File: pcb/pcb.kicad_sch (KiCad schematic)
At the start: 6 parts, among them U1 ESP32-S3, U2 LM337_TO220

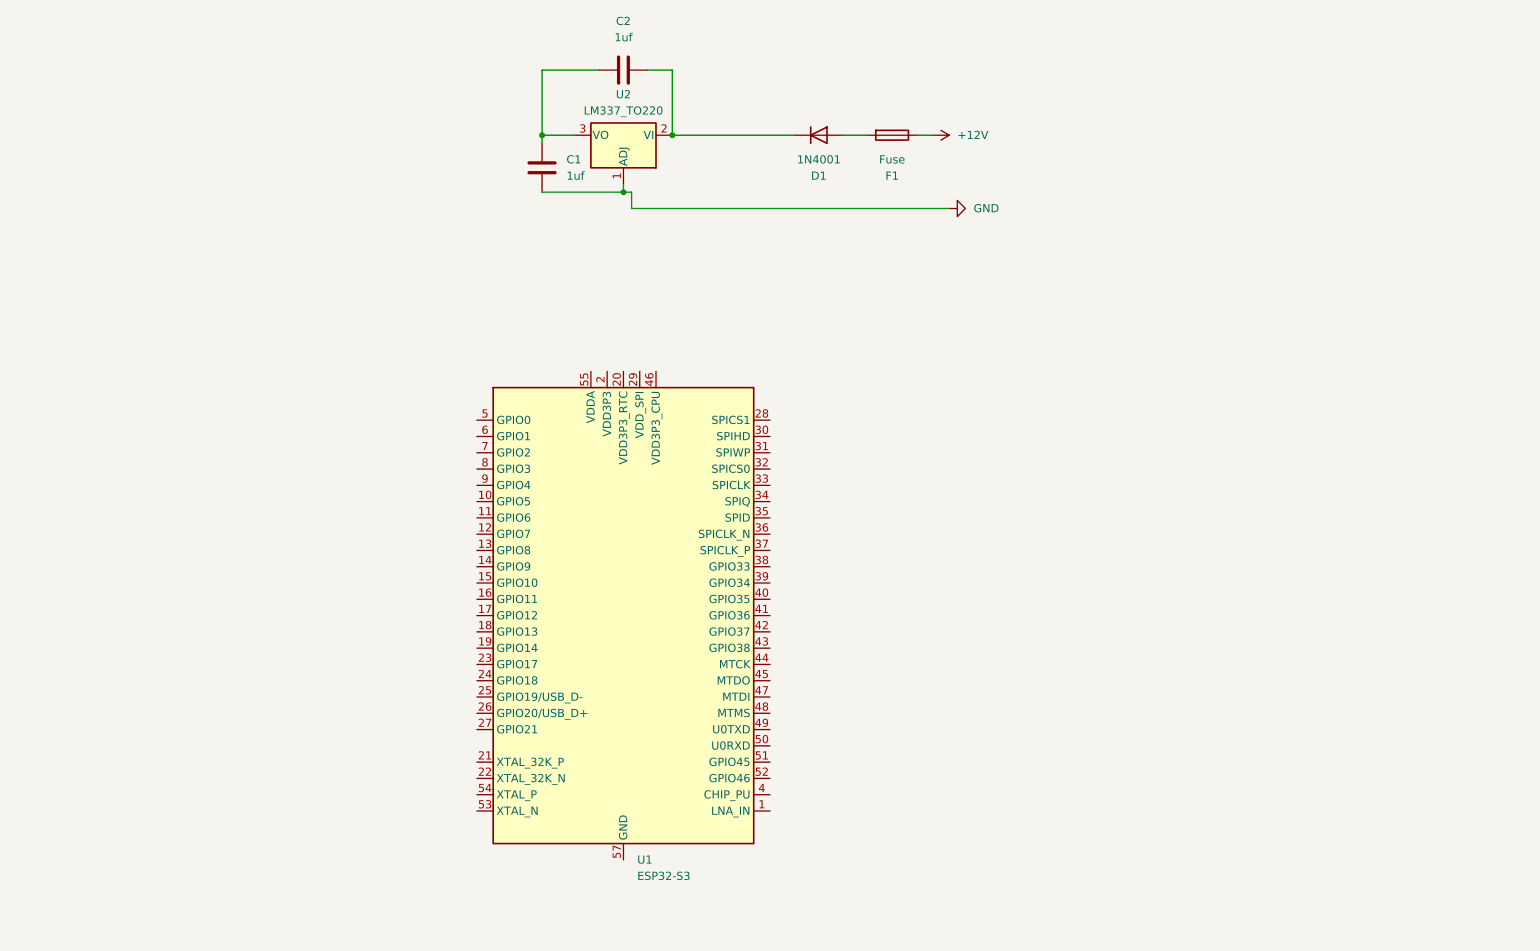
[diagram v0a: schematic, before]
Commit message: missed a wire, put more names for screw terminals
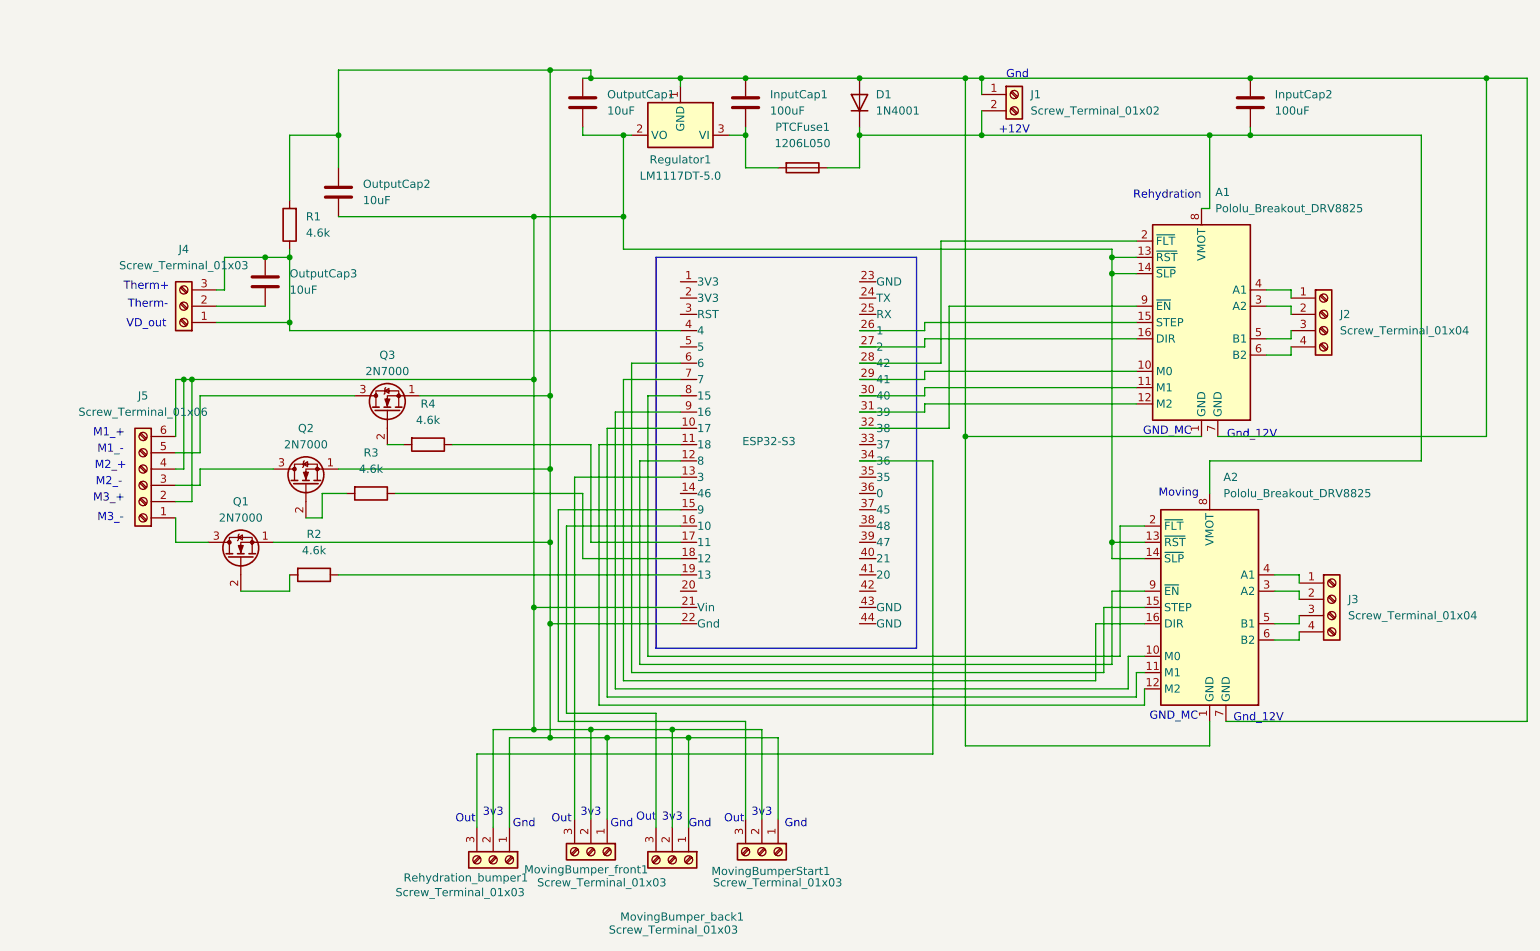
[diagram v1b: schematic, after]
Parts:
- removed C2: 1uf, Capacitor_SMD:C_01005_0402Metric, symbol Device:C
- removed U1: ESP32-S3, Package_DFN_QFN:QFN-56-1EP_7x7mm_P0.4mm_EP4x4mm, symbol MCU_Espressif:ESP32-S3
- removed U2: LM337_TO220, Package_TO_SOT_THT:TO-220-3_Vertical, symbol Regulator_Linear:LM337_TO220
- added A1, A2: Pololu_Breakout_DRV8825, Module:Pololu_Breakout-16_15.2x20.3mm, symbol Driver_Motor:Pololu_Breakout_DRV8825
- added ESP32-S3: ~, my_footprints:ESP32_DevKitC_Header_Mount, symbol symbol_libraru:ESP32-S3_DevKitC_dual_header
- added InputCap2: 100uF, Capacitor_SMD:C_0805_2012Metric, symbol Device:C
- added J1: Screw_Terminal_01x02, TerminalBlock:TerminalBlock_MaiXu_MX126-5.0-02P_1x02_P5.00mm, symbol Connector:Screw_Terminal_01x02
- added J2, J3: Screw_Terminal_01x04, TerminalBlock:TerminalBlock_MaiXu_MX126-5.0-04P_1x04_P5.00mm, symbol Connector:Screw_Terminal_01x04
- added J4, MovingBumperStart1, MovingBumper_back1, MovingBumper_front1, Rehydration_bumper1: Screw_Terminal_01x03, TerminalBlock:TerminalBlock_MaiXu_MX126-5.0-03P_1x03_P5.00mm, symbol Connector:Screw_Terminal_01x03
- added J5: Screw_Terminal_01x06, TerminalBlock:TerminalBlock_MaiXu_MX126-5.0-06P_1x06_P5.00mm, symbol Connector:Screw_Terminal_01x06
- added OutputCap1, OutputCap2, OutputCap3: 10uF, Capacitor_SMD:C_0805_2012Metric, symbol Device:C
- added Q1, Q2, Q3: 2N7000, Package_TO_SOT_THT:TO-92_Inline, symbol Transistor_FET:2N7000
- added R1, R2, R3, R4: 4.6k, Resistor_SMD:R_0805_2012Metric, symbol Device:R
- added Regulator1: LM1117DT-5.0, Package_TO_SOT_SMD:TO-252-3_TabPin2, symbol Regulator_Linear:LM1117DT-5.0
- InputCap1: renamed from C1; value 1uf -> 100uF; footprint Capacitor_SMD:C_01005_0402Metric -> Capacitor_SMD:C_0805_2012Metric
- PTCFuse1: renamed from F1; value Fuse -> 1206L050; footprint Fuse:Fuseholder_TR5_Littelfuse_No560_No460 -> Resistor_SMD:R_1206_3216Metric
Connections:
- net +12V is gone; now on an unnamed net: PTCFuse1.1
- net at D1.2 (A): now also InputCap1.1, A1.1 (GND), A1.7 (GND), A2.1 (GND), A2.7 (GND), ESP32-S3.22 (Gnd), InputCap2.1, J1.1 (Pin_1), MovingBumperStart1.1 (Pin_1), MovingBumper_back1.1 (Pin_1), MovingBumper_front1.1 (Pin_1), OutputCap1.1, OutputCap2.1, Q1.1 (S), Q2.1 (S), Q3.1 (S), R1.2, Regulator1.1 (GND), Rehydration_bumper1.1 (Pin_1); no longer PTCFuse1.2
- net at D1.1 (K): now also A1.8 (VMOT), A2.8 (VMOT), InputCap2.2, J1.2 (Pin_2)
- net GND: no longer names the net of InputCap1.2
- net GND: now also PTCFuse1.2, Regulator1.3 (VI)
- new net: A1.13 (~{RST}), A1.14 (~{SLP}), A2.13 (~{RST}), A2.14 (~{SLP}), ESP32-S3.21 (Vin), J5.2 (Pin_2), J5.4 (Pin_4), J5.6 (Pin_6), MovingBumperStart1.2 (Pin_2), MovingBumper_back1.2 (Pin_2), MovingBumper_front1.2 (Pin_2), OutputCap1.2, OutputCap2.2, Regulator1.2 (VO), Rehydration_bumper1.2 (Pin_2)
- new net: ESP32-S3.13 (3), MovingBumper_front1.3 (Pin_3)
- new net: ESP32-S3.34 (36), Rehydration_bumper1.3 (Pin_3)
- new net: Q2.2 (G), R3.2
- new net: J5.3 (Pin_3), Q2.3 (D)
- new net: ESP32-S3.19 (13), R2.1
- new net: Q1.2 (G), R2.2
- new net: ESP32-S3.15 (9), MovingBumperStart1.3 (Pin_3)
- new net: ESP32-S3.18 (12), R3.1
- new net: A2.11 (M1), ESP32-S3.10 (17)
- new net: A2.12 (M2), ESP32-S3.11 (18)
- new net: A2.9 (~{EN}), ESP32-S3.12 (8)
- new net: ESP32-S3.16 (10), MovingBumper_back1.3 (Pin_3)
- new net: ESP32-S3.17 (11), R4.1
- new net: A1.15 (STEP), ESP32-S3.26 (1)
- new net: A1.16 (DIR), ESP32-S3.27 (2)
- new net: A1.2 (~{FLT}), ESP32-S3.28 (42)
- new net: A1.10 (M0), ESP32-S3.29 (41)
- new net: A1.11 (M1), ESP32-S3.30 (40)
- new net: A1.12 (M2), ESP32-S3.31 (39)
- new net: A1.9 (~{EN}), ESP32-S3.32 (38)
- new net: ESP32-S3.4, J4.1 (Pin_1), J4.3 (Pin_3), OutputCap3.1, R1.1
- new net: A2.15 (STEP), ESP32-S3.6
- new net: A2.16 (DIR), ESP32-S3.7
- new net: A2.2 (~{FLT}), ESP32-S3.8 (15)
- new net: A2.10 (M0), ESP32-S3.9 (16)
- new net: A2.3 (A2), J3.2 (Pin_2)
- new net: A2.4 (A1), J3.1 (Pin_1)
- new net: A2.5 (B1), J3.3 (Pin_3)
- new net: A2.6 (B2), J3.4 (Pin_4)
- new net: A1.3 (A2), J2.2 (Pin_2)
- new net: A1.4 (A1), J2.1 (Pin_1)
- new net: A1.5 (B1), J2.3 (Pin_3)
- new net: A1.6 (B2), J2.4 (Pin_4)
- new net: Q3.2 (G), R4.2
- new net: J5.5 (Pin_5), Q3.3 (D)
- new net: J5.1 (Pin_1), Q1.3 (D)
- new net: J4.2 (Pin_2), OutputCap3.2
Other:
- note added: "+12V"
- note added: "3v3"
- note added: "GND_MC"
- note added: "Gnd"
- note added: "Gnd_12V"
- note added: "M1_+"
- note added: "M1_-"
- note added: "M2_+"
- note added: "M2_-"
- note added: "M3_+"
- note added: "M3_-"
- note added: "Moving"
- note added: "Out"
- note added: "Rehydration"
- note added: "Therm+"
- note added: "Therm-"
- note added: "VD_out"
- moved on the sheet: InputCap1, PTCFuse1

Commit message: new pcb file saved
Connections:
- net at A1.13 (~{RST}), A1.14 (~{SLP}), A2.13 (~{RST})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: now also ESP32-S3.1 (3V3); no longer ESP32-S3.21 (Vin), OutputCap1.2, Regulator1.2 (VO)
- net B_F: now reaches ESP32-S3.13 (3), MovingBumper_front1.3 (Pin_3)
- net Mix1: now reaches ESP32-S3.19 (13), R2.1
- net B_S: now reaches ESP32-S3.15 (9), MovingBumperStart1.3 (Pin_3)
- net Mix2: now reaches ESP32-S3.18 (12), R3.1
- net M1: now reaches A2.11 (M1), ESP32-S3.10 (17)
- net M2: now reaches A2.12 (M2), ESP32-S3.11 (18)
- net M0: now reaches A2.9 (~{EN}), ESP32-S3.12 (8)
- net M0: now also A2.10 (M0), ESP32-S3.9 (16)
- net B_B: now reaches ESP32-S3.16 (10), MovingBumper_back1.3 (Pin_3)
- net Mix3: now reaches ESP32-S3.17 (11), R4.1
- net VD_o: now reaches ESP32-S3.4, J4.1 (Pin_1), J4.3 (Pin_3), OutputCap3.1, R1.1
- net STEP: now reaches A2.15 (STEP), ESP32-S3.6
- net DIR: now reaches A2.16 (DIR), ESP32-S3.7
- net FLT: now reaches A2.2 (~{FLT}), ESP32-S3.8 (15)
- new net: ESP32-S3.21 (Vin), OutputCap1.2, Regulator1.2 (VO)

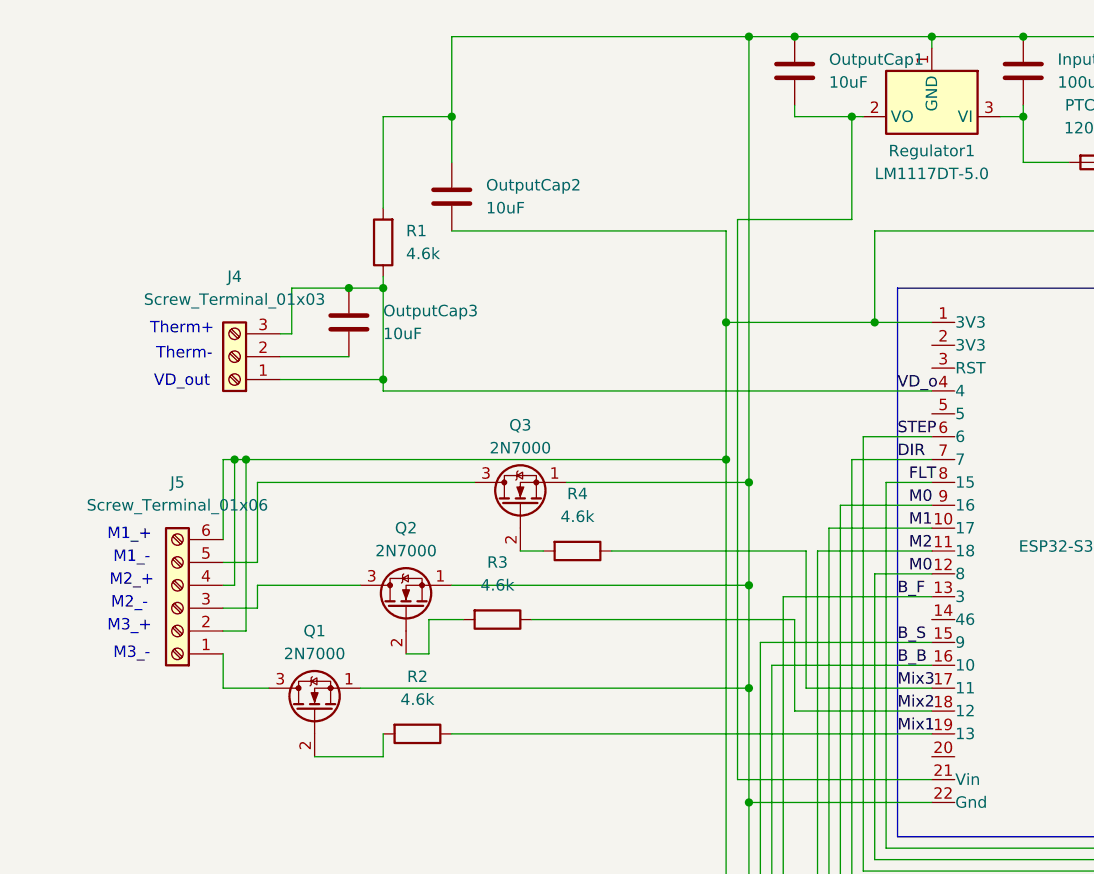
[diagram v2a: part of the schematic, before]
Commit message: fix voltage divider
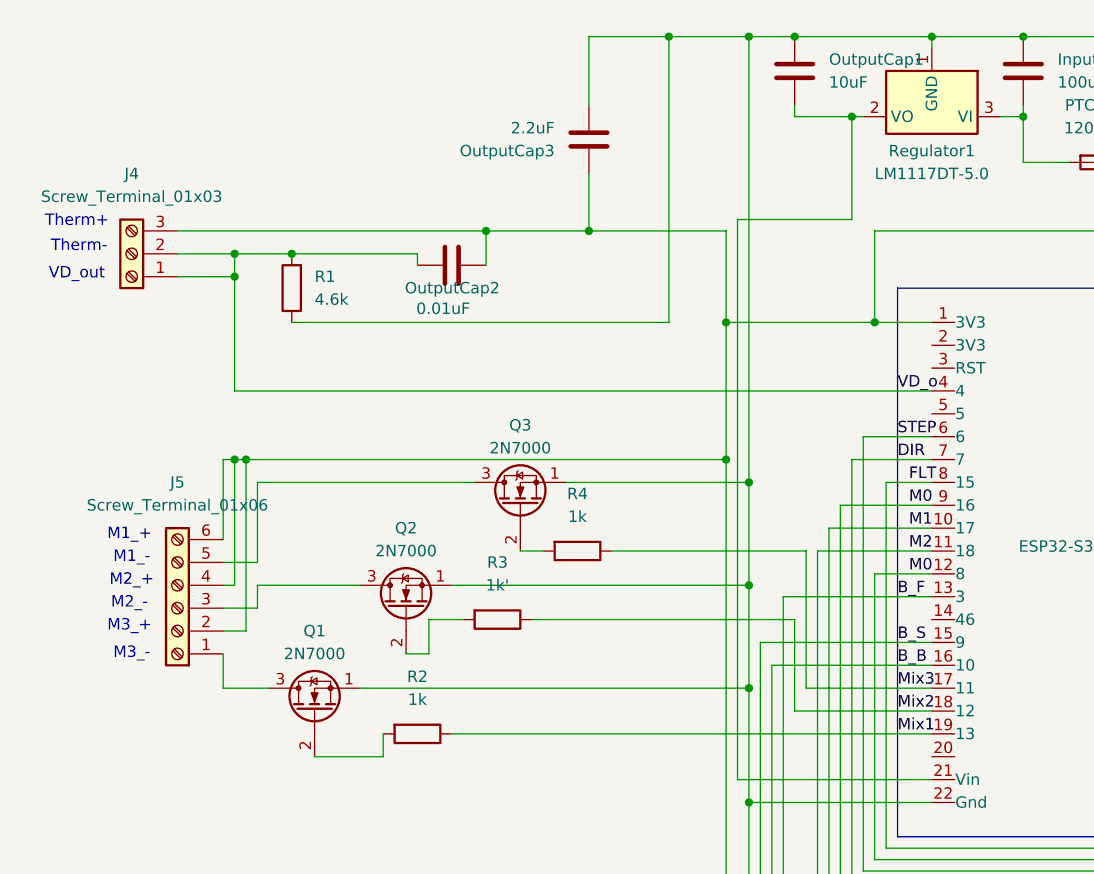
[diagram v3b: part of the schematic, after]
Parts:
- OutputCap2: value 10uF -> 0.01uF
- OutputCap3: value 10uF -> 2.2uF
- R2, R4: value 4.6k -> 1k
- R3: value 4.6k -> 1k'
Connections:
- net VD_o: now also J4.2 (Pin_2), OutputCap2.1, R1.2; no longer J4.3 (Pin_3), OutputCap3.1, R1.1
- net at A1.1 (GND), A1.7 (GND), A2.1 (GND)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: now also OutputCap3.2, R1.1; no longer OutputCap2.1, R1.2
- net at A1.13 (~{RST}), A1.14 (~{SLP}), A2.13 (~{RST})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: now also J4.3 (Pin_3), OutputCap3.1
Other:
- moved on the sheet: J4, OutputCap2, OutputCap3, R1

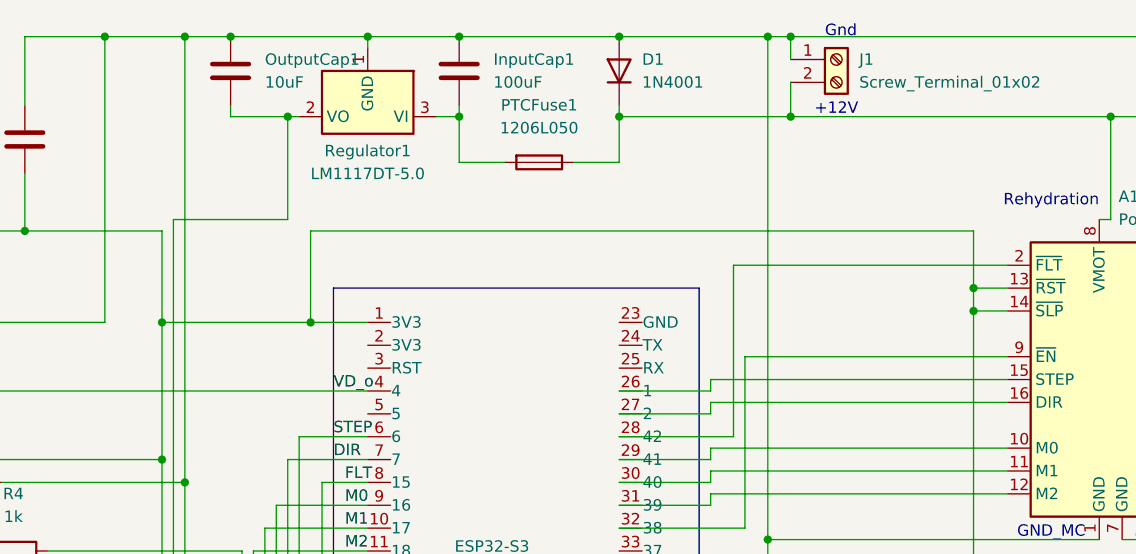
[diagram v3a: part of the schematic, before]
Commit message: fix motor controller input to 5V
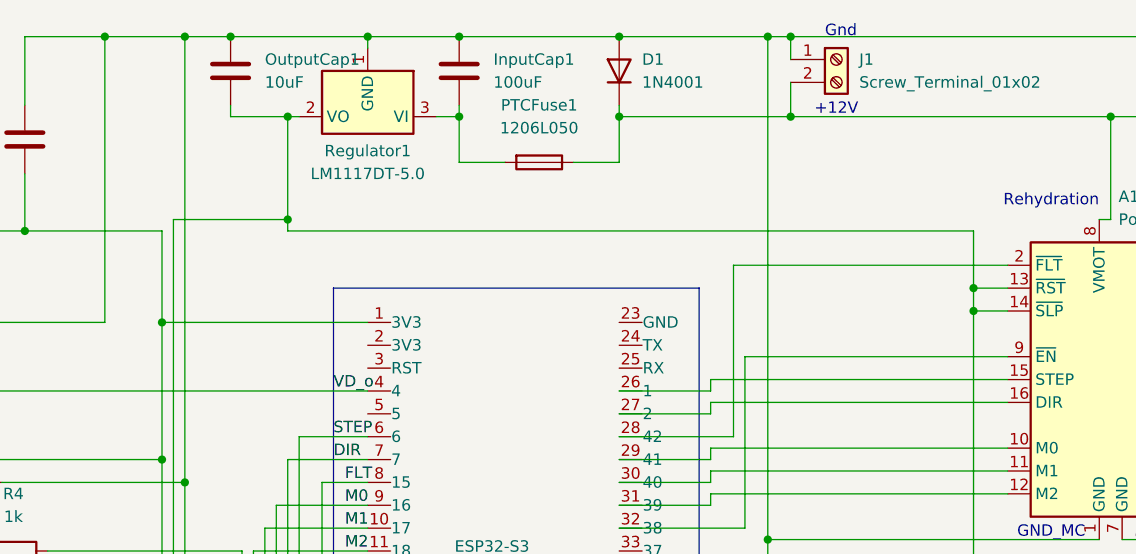
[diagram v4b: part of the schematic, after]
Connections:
- net at ESP32-S3.1 (3V3), J4.3 (Pin_3), J5.2 (Pin_2)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: no longer A1.13 (~{RST}), A1.14 (~{SLP}), A2.13 (~{RST}), A2.14 (~{SLP})
- net at ESP32-S3.21 (Vin), OutputCap1.2, Regulator1.2 (VO): now also A1.13 (~{RST}), A1.14 (~{SLP}), A2.13 (~{RST}), A2.14 (~{SLP})
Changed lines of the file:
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@@
+	)
+	(junction
+		(at 135.89 44.45)
+		(diameter 0)
+		(color 0 0 0 0)
 	)
 	(junction
@@
 	)
 	(junction
-		(at 138.43 55.88)
-		(diameter 0)
-		(color 0 0 0 0)
-	)
-	(junction
 		(at 124.46 96.52)
 		(diameter 0)
@@
 	(wire
 		(pts
-			(xy 212.09 45.72) (xy 138.43 45.72)
-		)
-		(stroke
-			(width 0)
-			(type default)
-		)
-	)
-	(wire
-		(pts
 			(xy 68.58 71.12) (xy 121.92 71.12)
 		)
@@
 	(wire
 		(pts
-			(xy 138.43 45.72) (xy 138.43 55.88)
-		)
-		(stroke
-			(width 0)
-			(type default)
-		)
-	)
-	(wire
-		(pts
 			(xy 66.04 71.12) (xy 67.31 71.12)
 		)
@@
 	(wire
 		(pts
+			(xy 135.89 44.45) (xy 135.89 45.72)
+		)
+		(stroke
+			(width 0)
+			(type default)
+		)
+	)
+	(wire
+		(pts
 			(xy 69.85 87.63) (xy 66.04 87.63)
 		)
@@
 	(wire
 		(pts
-			(xy 121.92 55.88) (xy 138.43 55.88)
+			(xy 121.92 55.88) (xy 144.78 55.88)
 		)
 		(stroke
@@
 	(wire
 		(pts
+			(xy 135.89 33.02) (xy 135.89 44.45)
+		)
+		(stroke
+			(width 0)
+			(type default)
+		)
+	)
+	(wire
+		(pts
 			(xy 215.9 120.65) (xy 133.35 120.65)
 		)
@@
 	(wire
 		(pts
-			(xy 135.89 33.02) (xy 135.89 44.45)
-		)
-		(stroke
-			(width 0)
-			(type default)
-		)
-	)
-	(wire
-		(pts
 			(xy 236.22 57.15) (xy 240.03 57.15)
 		)
@@
 	(wire
 		(pts
+			(xy 135.89 45.72) (xy 212.09 45.72)
+		)
+		(stroke
+			(width 0)
+			(type default)
+		)
+	)
+	(wire
+		(pts
 			(xy 172.72 76.2) (xy 182.88 76.2)
 		)
@@
 		)
 		(stroke
-			(width 0)
-			(type default)
-		)
-	)
-	(wire
-		(pts
-			(xy 138.43 55.88) (xy 144.78 55.88)
-		)
-		(stroke
